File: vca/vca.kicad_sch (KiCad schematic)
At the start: 52 parts, among them J1 Conn_01x03_Socket, J2 Conn_01x02_Socket, J3 Conn_01x02_Socket, J4 Conn_01x02_Socket, J5 Conn_01x03_Socket, J6 Conn_01x02_Socket, J7 Conn_01x02_Socket, J8 Conn_01x03_Socket, J9 Conn_01x02_Socket, Q1 BC548C, Q2 BC548C, Q3 BC548C, Q4 BC548C, U1 TL074

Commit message: use custom footprints with bigger pads
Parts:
- R1, R10, R11, R12, R13, R14, R15, R16, R17, R18, R19, R2, R20, R21, R22, R23, R24, R25, R26, R27, R28, R29, R3, R30, R31, R32, R4, R5, R6, R7, R8, R9: footprint Resistor_THT:R_Axial_DIN0204_L3.6mm_D1.6mm_P7.62mm_Horizontal -> my_library:my_tht_r
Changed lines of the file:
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@@
       (effects (font (size 1.27 1.27)))
     )
-    (property "Footprint" "Resistor_THT:R_Axial_DIN0204_L3.6mm_D1.6mm_P7.62mm_Horizontal" (at 54.102 124.968 90)
+    (property "Footprint" "my_library:my_tht_r" (at 54.102 124.968 90)
       (effects (font (size 1.27 1.27)) hide)
     )
@@
       (effects (font (size 1.27 1.27)))
     )
-    (property "Footprint" "Resistor_THT:R_Axial_DIN0204_L3.6mm_D1.6mm_P7.62mm_Horizontal" (at 215.646 103.632 90)
+    (property "Footprint" "my_library:my_tht_r" (at 215.646 103.632 90)
       (effects (font (size 1.27 1.27)) hide)
     )
@@
       (effects (font (size 1.27 1.27)))
     )
-    (property "Footprint" "Resistor_THT:R_Axial_DIN0204_L3.6mm_D1.6mm_P7.62mm_Horizontal" (at 152.146 150.622 90)
+    (property "Footprint" "my_library:my_tht_r" (at 152.146 150.622 90)
       (effects (font (size 1.27 1.27)) hide)
     )
@@
       (effects (font (size 1.27 1.27)) (justify left))
     )
-    (property "Footprint" "Resistor_THT:R_Axial_DIN0204_L3.6mm_D1.6mm_P7.62mm_Horizontal" (at 144.018 66.294 90)
+    (property "Footprint" "my_library:my_tht_r" (at 144.018 66.294 90)
       (effects (font (size 1.27 1.27)) hide)
     )
@@
       (effects (font (size 1.27 1.27)))
     )
-    (property "Footprint" "Resistor_THT:R_Axial_DIN0204_L3.6mm_D1.6mm_P7.62mm_Horizontal" (at 116.078 62.23 90)
+    (property "Footprint" "my_library:my_tht_r" (at 116.078 62.23 90)
       (effects (font (size 1.27 1.27)) hide)
     )
@@
       (effects (font (size 1.27 1.27)))
     )
-    (property "Footprint" "Resistor_THT:R_Axial_DIN0204_L3.6mm_D1.6mm_P7.62mm_Horizontal" (at 127.762 172.974 90)
+    (property "Footprint" "my_library:my_tht_r" (at 127.762 172.974 90)
       (effects (font (size 1.27 1.27)) hide)
     )
@@
       (effects (font (size 1.27 1.27)))
     )
-    (property "Footprint" "Resistor_THT:R_Axial_DIN0204_L3.6mm_D1.6mm_P7.62mm_Horizontal" (at 49.784 68.072 90)
+    (property "Footprint" "my_library:my_tht_r" (at 49.784 68.072 90)
       (effects (font (size 1.27 1.27)) hide)
     )
@@
       (effects (font (size 1.27 1.27)))
     )
-    (property "Footprint" "Resistor_THT:R_Axial_DIN0204_L3.6mm_D1.6mm_P7.62mm_Horizontal" (at 238.506 106.172 90)
+    (property "Footprint" "my_library:my_tht_r" (at 238.506 106.172 90)
       (effects (font (size 1.27 1.27)) hide)
     )
@@
       (effects (font (size 1.27 1.27)) (justify right))
     )
-    (property "Footprint" "Resistor_THT:R_Axial_DIN0204_L3.6mm_D1.6mm_P7.62mm_Horizontal" (at 100.79 73.152 90)
+    (property "Footprint" "my_library:my_tht_r" (at 100.79 73.152 90)
       (effects (font (size 1.27 1.27)) hide)
     )
@@
       (effects (font (size 1.27 1.27)) (justify right))
     )
-    (property "Footprint" "Resistor_THT:R_Axial_DIN0204_L3.6mm_D1.6mm_P7.62mm_Horizontal" (at 174.45 121.158 90)
+    (property "Footprint" "my_library:my_tht_r" (at 174.45 121.158 90)
       (effects (font (size 1.27 1.27)) hide)
     )
@@
       (effects (font (size 1.27 1.27)))
     )
-    (property "Footprint" "Resistor_THT:R_Axial_DIN0204_L3.6mm_D1.6mm_P7.62mm_Horizontal" (at 164.846 58.166 90)
+    (property "Footprint" "my_library:my_tht_r" (at 164.846 58.166 90)
       (effects (font (size 1.27 1.27)) hide)
     )
@@
       (effects (font (size 1.27 1.27)) (justify left))
     )
-    (property "Footprint" "Resistor_THT:R_Axial_DIN0204_L3.6mm_D1.6mm_P7.62mm_Horizontal" (at 184.15 115.824 90)
+    (property "Footprint" "my_library:my_tht_r" (at 184.15 115.824 90)
       (effects (font (size 1.27 1.27)) hide)
     )
@@
       (effects (font (size 1.27 1.27)) (justify left))
     )
-    (property "Footprint" "Resistor_THT:R_Axial_DIN0204_L3.6mm_D1.6mm_P7.62mm_Horizontal" (at 48.514 120.396 90)
+    (property "Footprint" "my_library:my_tht_r" (at 48.514 120.396 90)
       (effects (font (size 1.27 1.27)) hide)
     )
@@
       (effects (font (size 1.27 1.27)))
     )
-    (property "Footprint" "Resistor_THT:R_Axial_DIN0204_L3.6mm_D1.6mm_P7.62mm_Horizontal" (at 123.444 116.078 90)
+    (property "Footprint" "my_library:my_tht_r" (at 123.444 116.078 90)
       (effects (font (size 1.27 1.27)) hide)
     )
@@
       (effects (font (size 1.27 1.27)))
     )
-    (property "Footprint" "Resistor_THT:R_Axial_DIN0204_L3.6mm_D1.6mm_P7.62mm_Horizontal" (at 225.298 94.742 90)
+    (property "Footprint" "my_library:my_tht_r" (at 225.298 94.742 90)
       (effects (font (size 1.27 1.27)) hide)
     )
@@
       (effects (font (size 1.27 1.27)) (justify left))
     )
-    (property "Footprint" "Resistor_THT:R_Axial_DIN0204_L3.6mm_D1.6mm_P7.62mm_Horizontal" (at 110.49 67.818 90)
+    (property "Footprint" "my_library:my_tht_r" (at 110.49 67.818 90)
       (effects (font (size 1.27 1.27)) hide)
     )
@@
       (effects (font (size 1.27 1.27)) (justify right))
     )
-    (property "Footprint" "Resistor_THT:R_Axial_DIN0204_L3.6mm_D1.6mm_P7.62mm_Horizontal" (at 129.032 110.49 90)
+    (property "Footprint" "my_library:my_tht_r" (at 129.032 110.49 90)
       (effects (font (size 1.27 1.27)) hide)
     )
@@
       (effects (font (size 1.27 1.27)))
     )
-    (property "Footprint" "Resistor_THT:R_Axial_DIN0204_L3.6mm_D1.6mm_P7.62mm_Horizontal" (at 189.738 110.236 90)
+    (property "Footprint" "my_library:my_tht_r" (at 189.738 110.236 90)
       (effects (font (size 1.27 1.27)) hide)
     )
@@
       (effects (font (size 1.27 1.27)) (justify right))
     )
-    (property "Footprint" "Resistor_THT:R_Axial_DIN0204_L3.6mm_D1.6mm_P7.62mm_Horizontal" (at 166.116 103.378 90)
+    (property "Footprint" "my_library:my_tht_r" (at 166.116 103.378 90)
       (effects (font (size 1.27 1.27)) hide)
     )
@@
       (effects (font (size 1.27 1.27)))
     )
-    (property "Footprint" "Resistor_THT:R_Axial_DIN0204_L3.6mm_D1.6mm_P7.62mm_Horizontal" (at 78.486 102.616 90)
+    (property "Footprint" "my_library:my_tht_r" (at 78.486 102.616 90)
       (effects (font (size 1.27 1.27)) hide)
     )
@@
       (effects (font (size 1.27 1.27)) (justify right))
     )
-    (property "Footprint" "Resistor_THT:R_Axial_DIN0204_L3.6mm_D1.6mm_P7.62mm_Horizontal" (at 108.966 55.118 90)
+    (property "Footprint" "my_library:my_tht_r" (at 108.966 55.118 90)
       (effects (font (size 1.27 1.27)) hide)
     )
@@
       (effects (font (size 1.27 1.27)))
     )
-    (property "Footprint" "Resistor_THT:R_Axial_DIN0204_L3.6mm_D1.6mm_P7.62mm_Horizontal" (at 141.986 55.626 90)
+    (property "Footprint" "my_library:my_tht_r" (at 141.986 55.626 90)
       (effects (font (size 1.27 1.27)) hide)
     )
@@
       (effects (font (size 1.27 1.27)) (justify right))
     )
-    (property "Footprint" "Resistor_THT:R_Axial_DIN0204_L3.6mm_D1.6mm_P7.62mm_Horizontal" (at 182.626 103.124 90)
+    (property "Footprint" "my_library:my_tht_r" (at 182.626 103.124 90)
       (effects (font (size 1.27 1.27)) hide)
     )
@@
       (effects (font (size 1.27 1.27)))
     )
-    (property "Footprint" "Resistor_THT:R_Axial_DIN0204_L3.6mm_D1.6mm_P7.62mm_Horizontal" (at 215.646 108.712 90)
+    (property "Footprint" "my_library:my_tht_r" (at 215.646 108.712 90)
       (effects (font (size 1.27 1.27)) hide)
     )
@@
       (effects (font (size 1.27 1.27)))
     )
-    (property "Footprint" "Resistor_THT:R_Axial_DIN0204_L3.6mm_D1.6mm_P7.62mm_Horizontal" (at 151.638 46.736 90)
+    (property "Footprint" "my_library:my_tht_r" (at 151.638 46.736 90)
       (effects (font (size 1.27 1.27)) hide)
     )
@@
       (effects (font (size 1.27 1.27)))
     )
-    (property "Footprint" "Resistor_THT:R_Axial_DIN0204_L3.6mm_D1.6mm_P7.62mm_Horizontal" (at 135.89 141.224 90)
+    (property "Footprint" "my_library:my_tht_r" (at 135.89 141.224 90)
       (effects (font (size 1.27 1.27)) hide)
     )
@@
       (effects (font (size 1.27 1.27)))
     )
-    (property "Footprint" "Resistor_THT:R_Axial_DIN0204_L3.6mm_D1.6mm_P7.62mm_Horizontal" (at 141.986 60.706 90)
+    (property "Footprint" "my_library:my_tht_r" (at 141.986 60.706 90)
       (effects (font (size 1.27 1.27)) hide)
     )
@@
       (effects (font (size 1.27 1.27)) (justify right))
     )
-    (property "Footprint" "Resistor_THT:R_Axial_DIN0204_L3.6mm_D1.6mm_P7.62mm_Horizontal" (at 55.372 62.484 90)
+    (property "Footprint" "my_library:my_tht_r" (at 55.372 62.484 90)
       (effects (font (size 1.27 1.27)) hide)
     )
@@
       (effects (font (size 1.27 1.27)) (justify left))
     )
-    (property "Footprint" "Resistor_THT:R_Axial_DIN0204_L3.6mm_D1.6mm_P7.62mm_Horizontal" (at 122.174 168.402 90)
+    (property "Footprint" "my_library:my_tht_r" (at 122.174 168.402 90)
       (effects (font (size 1.27 1.27)) hide)
     )
@@
       (effects (font (size 1.27 1.27)))
     )
-    (property "Footprint" "Resistor_THT:R_Axial_DIN0204_L3.6mm_D1.6mm_P7.62mm_Horizontal" (at 62.23 93.218 90)
+    (property "Footprint" "my_library:my_tht_r" (at 62.23 93.218 90)
       (effects (font (size 1.27 1.27)) hide)
     )
@@
       (effects (font (size 1.27 1.27)) (justify left))
     )
-    (property "Footprint" "Resistor_THT:R_Axial_DIN0204_L3.6mm_D1.6mm_P7.62mm_Horizontal" (at 217.678 114.3 90)
+    (property "Footprint" "my_library:my_tht_r" (at 217.678 114.3 90)
       (effects (font (size 1.27 1.27)) hide)
     )
@@
       (effects (font (size 1.27 1.27)) (justify right))
     )
-    (property "Footprint" "Resistor_THT:R_Axial_DIN0204_L3.6mm_D1.6mm_P7.62mm_Horizontal" (at 92.456 55.372 90)
-      (effects (font (size 1.27 1.27)) hide)
-    )
+    (property "Footprint" "my_library:my_tht_r" (at 92.456 55.372 90)
+      (effects (font (size 1.27 1.27)) hide)
+    )

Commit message: update almost all other footprints to fatty pads
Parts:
- Q1, Q2, Q3, Q4: footprint BC548C:TO92250P510H770-3 -> my_library:my_bc548
- RV1, RV2: footprint Potentiometer_THT:Potentiometer_Vishay_T73XW_Horizontal -> my_library:my_trimmer
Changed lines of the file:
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@@
       (effects (font (size 1.27 1.27)) (justify left))
     )
-    (property "Footprint" "BC548C:TO92250P510H770-3" (at 183.388 112.014 0)
+    (property "Footprint" "my_library:my_bc548" (at 183.388 112.014 0)
       (effects (font (size 1.27 1.27)) (justify bottom) hide)
     )
@@
       (effects (font (size 1.27 1.27)) (justify left))
     )
-    (property "Footprint" "BC548C:TO92250P510H770-3" (at 109.728 64.008 0)
+    (property "Footprint" "my_library:my_bc548" (at 109.728 64.008 0)
       (effects (font (size 1.27 1.27)) (justify bottom) hide)
     )
@@
       (effects (font (size 1.27 1.27)))
     )
-    (property "Footprint" "Potentiometer_THT:Potentiometer_Vishay_T73XW_Horizontal" (at 129.794 70.866 0)
+    (property "Footprint" "my_library:my_trimmer" (at 129.794 70.866 0)
       (effects (font (size 1.27 1.27)) hide)
     )
@@
       (effects (font (size 1.27 1.27)) (justify left))
     )
-    (property "Footprint" "BC548C:TO92250P510H770-3" (at 88.138 64.262 0)
+    (property "Footprint" "my_library:my_bc548" (at 88.138 64.262 0)
       (effects (font (size 1.27 1.27)) (justify bottom) hide)
     )
@@
       (effects (font (size 1.27 1.27)) (justify left))
     )
-    (property "Footprint" "BC548C:TO92250P510H770-3" (at 161.798 112.268 0)
+    (property "Footprint" "my_library:my_bc548" (at 161.798 112.268 0)
       (effects (font (size 1.27 1.27)) (justify bottom) hide)
     )
@@
       (effects (font (size 1.27 1.27)))
     )
-    (property "Footprint" "Potentiometer_THT:Potentiometer_Vishay_T73XW_Horizontal" (at 203.454 118.872 0)
-      (effects (font (size 1.27 1.27)) hide)
-    )
+    (property "Footprint" "my_library:my_trimmer" (at 203.454 118.872 0)
+      (effects (font (size 1.27 1.27)) hide)
+    )

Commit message: FRIENDSHIP ENDED WITH PACKAGE_DIP. added a keep-out on F.cu for dip14
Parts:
- U1: footprint my_library:my_dip14 -> my_library:my_dip14_no_f_pads
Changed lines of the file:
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@@
       (effects (font (size 1.27 1.27)) (justify left))
     )
-    (property "Footprint" "my_library:my_dip14" (at 270.51 48.006 0)
+    (property "Footprint" "my_library:my_dip14_no_f_pads" (at 270.51 48.006 0)
       (effects (font (size 1.27 1.27)) hide)
     )
@@
       (effects (font (size 1.27 1.27)))
     )
-    (property "Footprint" "my_library:my_dip14" (at 77.47 114.046 0)
+    (property "Footprint" "my_library:my_dip14_no_f_pads" (at 77.47 114.046 0)
       (effects (font (size 1.27 1.27)) hide)
     )
@@
       (effects (font (size 1.27 1.27)))
     )
-    (property "Footprint" "my_library:my_dip14" (at 225.806 105.41 0)
+    (property "Footprint" "my_library:my_dip14_no_f_pads" (at 225.806 105.41 0)
       (effects (font (size 1.27 1.27)) hide)
     )
@@
       (effects (font (size 1.27 1.27)))
     )
-    (property "Footprint" "my_library:my_dip14" (at 152.146 57.404 0)
+    (property "Footprint" "my_library:my_dip14_no_f_pads" (at 152.146 57.404 0)
       (effects (font (size 1.27 1.27)) hide)
     )
@@
       (effects (font (size 1.27 1.27)))
     )
-    (property "Footprint" "my_library:my_dip14" (at 151.13 162.052 0)
-      (effects (font (size 1.27 1.27)) hide)
-    )
+    (property "Footprint" "my_library:my_dip14_no_f_pads" (at 151.13 162.052 0)
+      (effects (font (size 1.27 1.27)) hide)
+    )

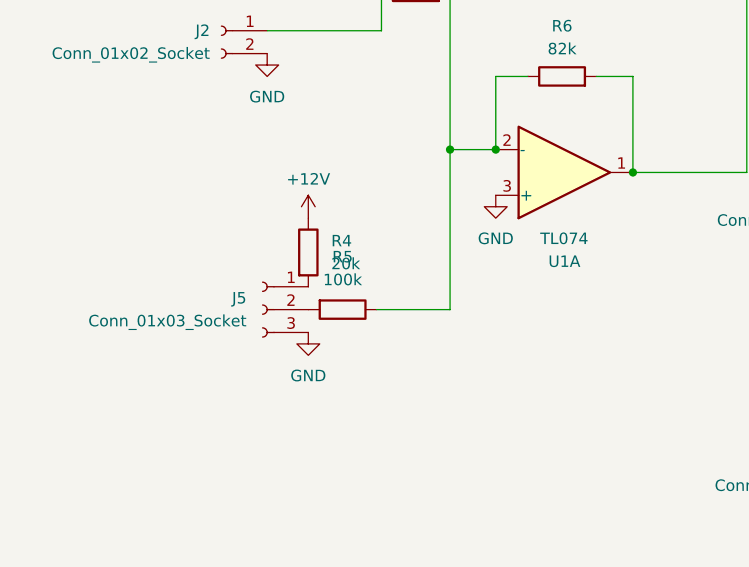
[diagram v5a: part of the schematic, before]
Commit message: some notes about front panel construction and some boms
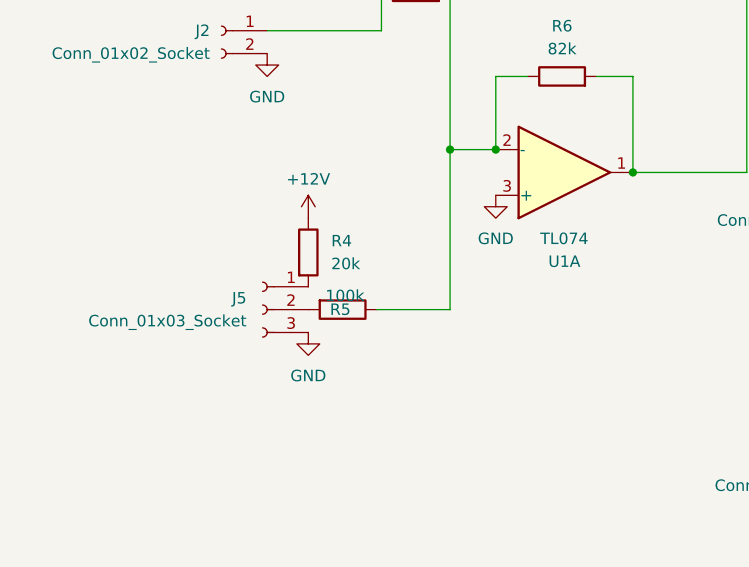
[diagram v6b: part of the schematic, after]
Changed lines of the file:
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@@
   )
   (symbol (lib_id "Device:R") (at 54.102 126.746 270) (unit 1)
-    (in_bom yes) (on_board yes) (dnp no) (fields_autoplaced)
-    (property "Reference" "R5" (at 54.102 120.904 90)
+    (in_bom yes) (on_board yes) (dnp no)
+    (property "Reference" "R5" (at 53.848 126.746 90)
       (effects (font (size 1.27 1.27)))
     )
-    (property "Value" "100k" (at 54.102 123.444 90)
+    (property "Value" "100k" (at 54.356 125.222 90)
       (effects (font (size 1.27 1.27)))
     )
